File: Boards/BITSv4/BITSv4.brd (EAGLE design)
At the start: 50 x 44.7 mm, 32 parts, among them U1 LMR16020, X1 53261-10

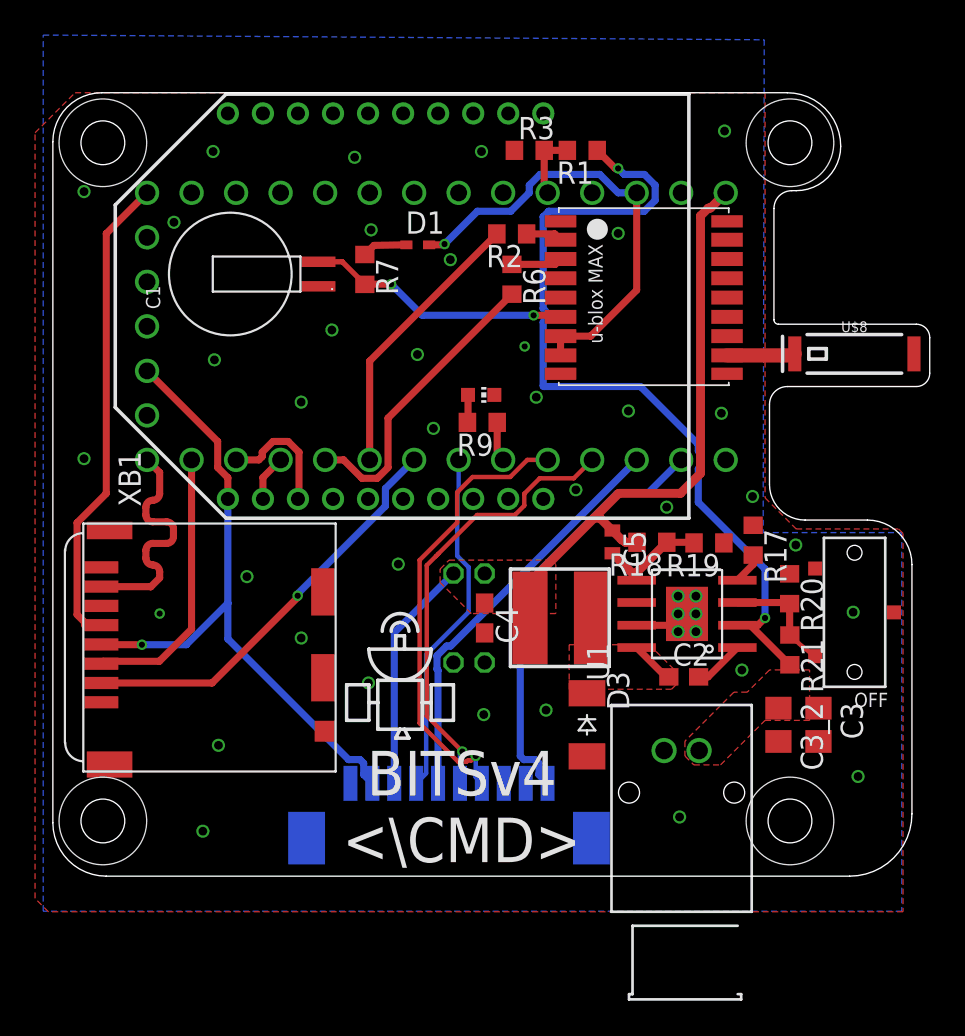
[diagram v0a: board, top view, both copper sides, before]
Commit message: LED reposition
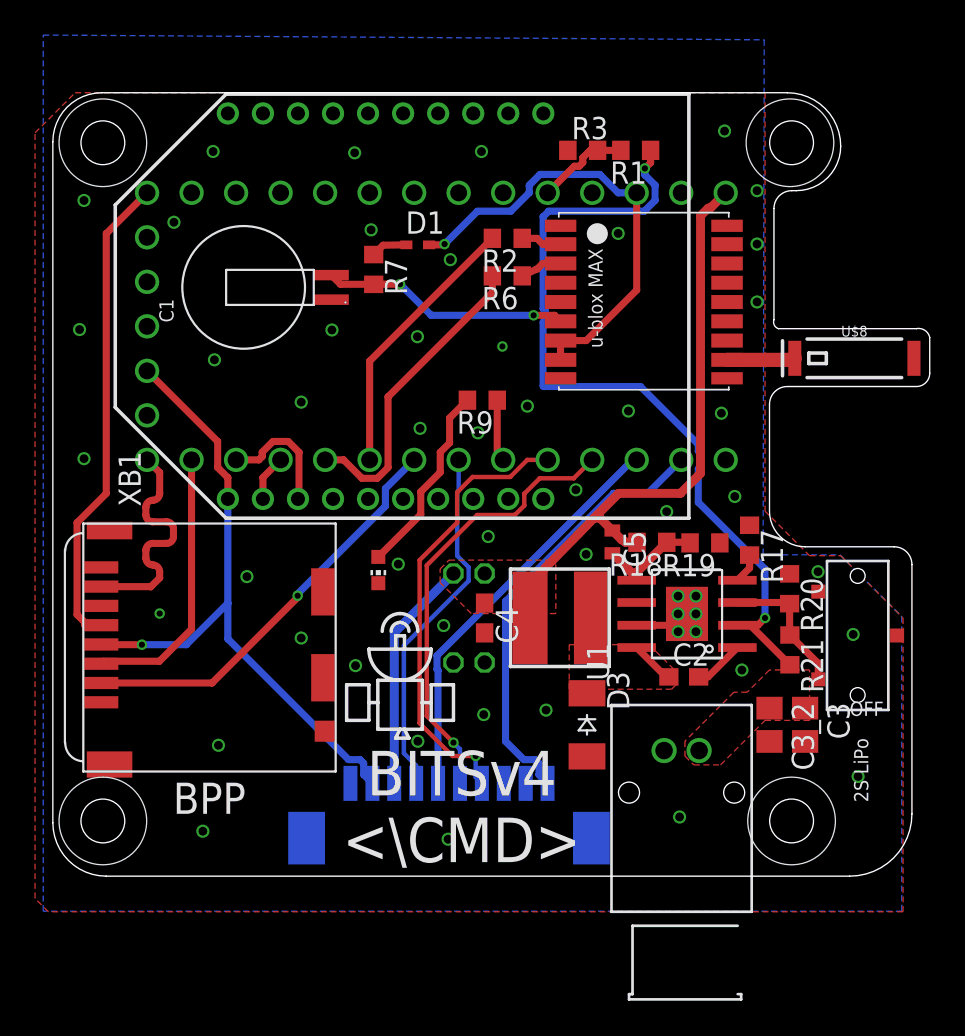
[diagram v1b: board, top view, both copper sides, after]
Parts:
- moved LED1 11.6 mm to (37.1, 13.2), turned to 180 degrees
- moved R1 3.05 mm to (51.8, 37.1)
- moved R3 3.05 mm to (48.8, 37.1)
- moved U$3 1.33 mm to (66.2, 13.7)
- moved R9 1.27 mm to (43.0, 22.8)
- moved C1 1.08 mm to (32.9, 29.3)
- moved C3 0.76 mm to (61.5, 4.32)
- moved C3_2 0.51 mm to (59.4, 4.32)
- moved R7 0.51 mm to (36.9, 30.3)
- moved R2 0.36 mm to (44.5, 32.1)
- moved R6 0.33 mm to (44.5, 29.9), turned to 180 degrees
- moved U$7 0.25 mm to (52.5, 28.4)
- moved U$8 0.25 mm to (64.3, 25.2)
- moved R19 0.23 mm to (55.8, 14.7)
- moved R17 0.20 mm to (58.3, 14.9)
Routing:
- net N$6: track 1.59 -> 11.0 mm
- net +5V: track 49.5 -> 47.4 mm
- net IN1: track 48.2 -> 46.5 mm
- net BAT_CELL1: track 3.83 -> 5.34 mm
- net N$7: track 6.68 -> 8.00 mm
- net LED1: track 2.28 -> 3.55 mm
- net V_BCKP: track 15.2 -> 14.2 mm
- net RXD: track 24.3 -> 25.1 mm
- net TX3: track 17.1 -> 17.7 mm
- net SLEEP: track 20.0 -> 20.6 mm
- net N$2: track 2.59 -> 2.08 mm
- net GND: vias 42 -> 52
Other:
- outline, holes or cut-outs redrawn
- board text removed: "</CMD>"

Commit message: connector move
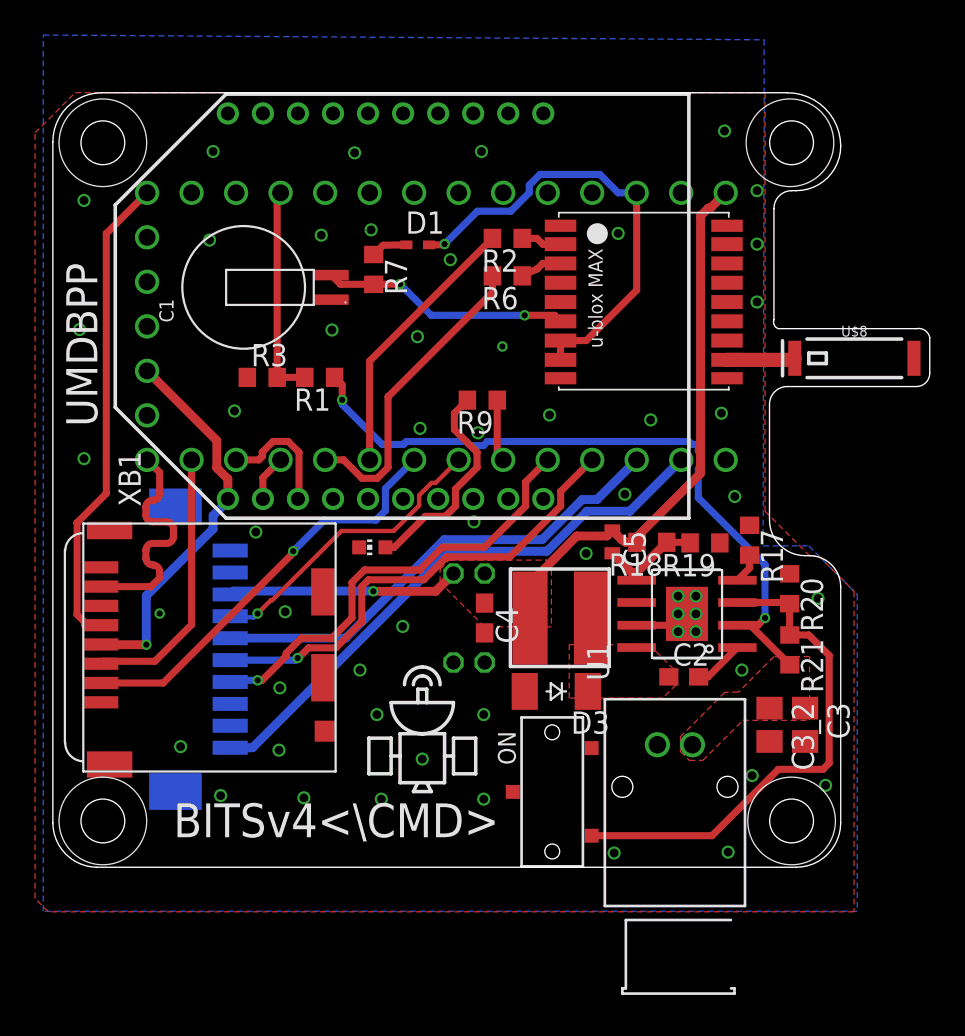
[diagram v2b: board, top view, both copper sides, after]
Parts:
- moved U$3 27.2 mm to (45.3, -3.76), turned to 90 degrees
- moved R3 22.4 mm to (30.5, 24.1)
- moved R1 22.2 mm to (33.8, 24.1)
- moved X1 18.1 mm to (26.2, 8.64), turned to 270 degrees
- moved D3 2.59 mm to (47.3, 6.22), turned to 180 degrees
- moved LED1 1.34 mm to (36.8, 14.4), turned to 90 degrees
- moved U$1 0.50 mm to (58.0, -6.02)
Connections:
- new net +3V3_LION: X1.9
- net +3V3: no longer X1.9
- net BAT_CELL1: now also U$2.16/A2; no longer U$2.22/A8
- net N$7: now also U$3.P$1; no longer U$3.P$3
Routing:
- net N$7: track 8.00 -> 28.9 mm
- net +3V3: track 63.9 -> 48.5 mm
- net RXD: track 25.1 -> 32.5 mm
- net BAT_CELL1: track 5.34 -> 12.2 mm
- net IN1: track 46.5 -> 39.8 mm
- net TXD: track 23.3 -> 27.4 mm
- net SLEEP: track 20.6 -> 17.1 mm, vias 0 -> 1
- net +5V: track 47.4 -> 45.0 mm, vias 0 -> 1
- net SW: track 2.53 -> 0.17 mm
- net RING: track 25.6 -> 27.1 mm
- net N$6: track 11.0 -> 12.4 mm
- net GND: vias 52 -> 55
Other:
- board size 50 x 44.7 mm -> 50 x 44.2 mm
- board text added: "BITSv4<\\CMD>"
- board text added: "ON"
- board text added: "UMDBPP"
- board text removed: "BITSv4 <\CMD>"
- board text removed: "BPP"
- board text removed: "OFF"

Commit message: TextMove
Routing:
- net GND: vias 55 -> 52
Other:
- board text added: "<3V3"
- board text added: "<5V"
- board text added: "Designed Q3 2021 J. Molter M. Kalin"
- board text added: "GND"
- board text removed: "3V3>"
- board text removed: "Isolated Conn GND IN_B OUT_A 3V3"
